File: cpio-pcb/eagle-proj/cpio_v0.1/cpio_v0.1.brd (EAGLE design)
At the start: 100 x 80 mm, 106 parts

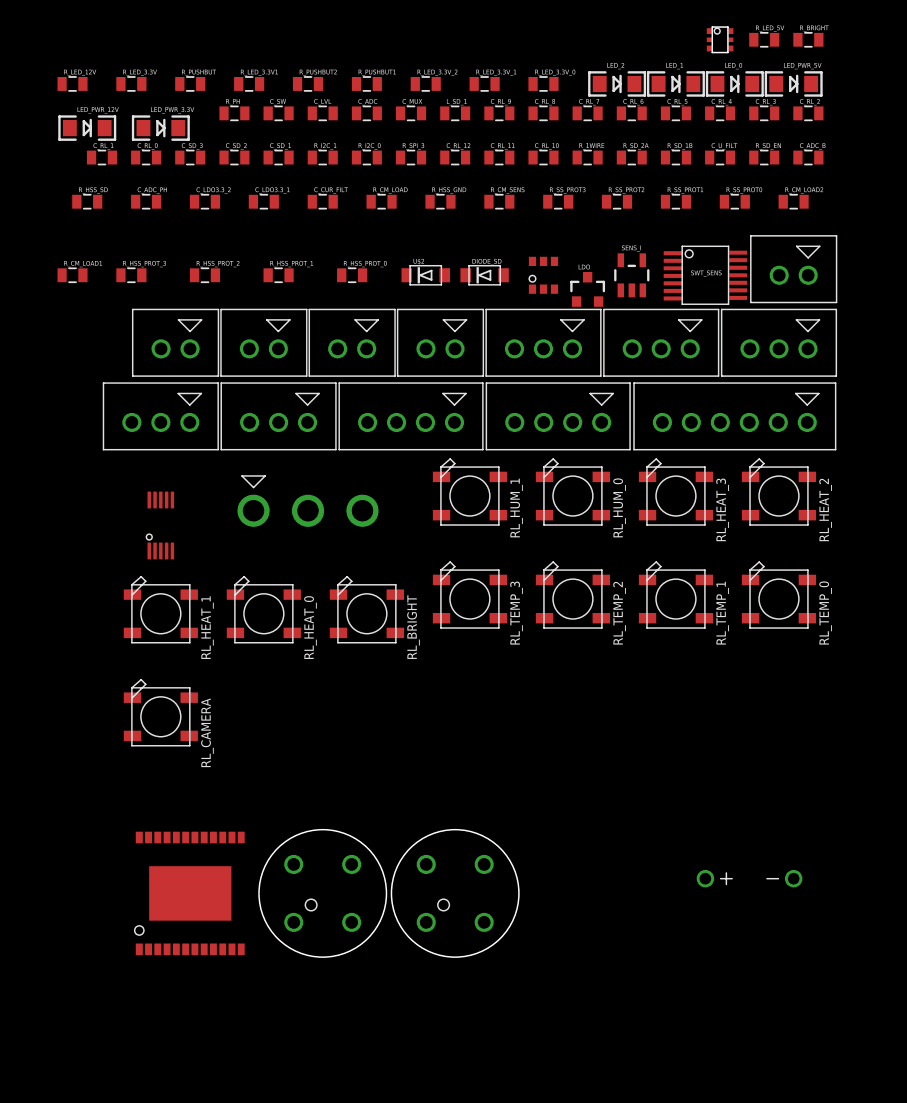
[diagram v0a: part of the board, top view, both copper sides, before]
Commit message: schematic review: button and some R less
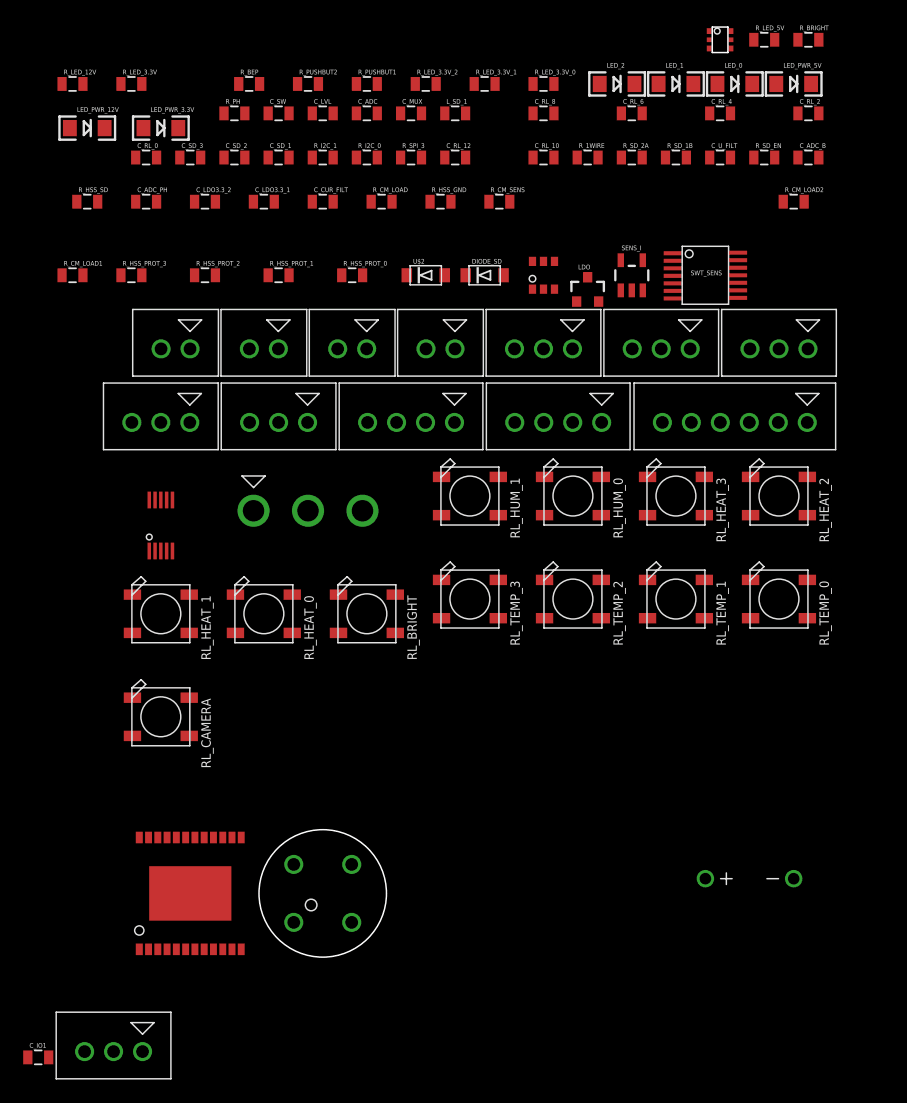
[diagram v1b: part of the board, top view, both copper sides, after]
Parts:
- removed C_RL_1, C_RL_11, C_RL_3, C_RL_5, C_RL_7, C_RL_9: 100n, SparkFun-Passives:0805
- removed PUSH: BUTTON, cpio:BUTTON
- removed R_PUSHBUT: (no value), SparkFun-Passives:0805
- removed R_SS_PROT0, R_SS_PROT1, R_SS_PROT2, R_SS_PROT3: 1k, SparkFun-Passives:0805
- removed SENS_BRIGHT: XH-A-2, cpio:XH-A-2
- added C_IO1: 100n, SparkFun-Passives:0805
- added SENS_PH1: XH-A-3, cpio:XH-A-3
- renumbered R_LED_3.3V1 to R_BEP
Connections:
- removed net GPIO_XXXXX: PUSH.1, PUSH.3
- removed net N$20: R_SS_PROT1.2, SWT_SENS.4
- removed net N$21: R_SS_PROT2.2, SWT_SENS.10
- removed net N$22: R_SS_PROT3.2, SWT_SENS.13
- removed net N$25: C_RL_12.1, R_PUSHBUT2.1
- removed net N$57: PUSH.2, PUSH.4, R_PUSHBUT.1
- new net GPIO_27: C_RL_12.1, R_PUSHBUT1.1, R_PUSHBUT2.2
- net 3.3V: now also C_IO1.1, SENS_PH.1, SENS_PH1.1; no longer R_PUSHBUT.2
- net 5V: no longer C_RL_1.1, C_RL_11.1, C_RL_3.1, C_RL_5.1, C_RL_7.1, C_RL_9.1
- net GND: now also C_IO1.2, SENS_PH.3, SENS_PH1.3; no longer C_RL_1.2, C_RL_11.2, C_RL_3.2, C_RL_5.2, C_RL_7.2, C_RL_9.2, SENS_BRIGHT.2
- net GPIO12: now also SWT_SENS.10; no longer R_SS_PROT2.1
- net GPIO16: now also SWT_SENS.4; no longer R_SS_PROT1.1
- net GPIO20: now also SWT_SENS.1; no longer R_SS_PROT0.1
- net GPIO25: now also SWT_SENS.13; no longer R_SS_PROT3.1
- net N$14: now also RL_HUM_0.4-DIN; no longer R_SS_PROT0.2, SWT_SENS.1
- net N$35: now also SENS_PH1.2; no longer SENS_BRIGHT.1
- net N$5: now also R_PUSHBUT2.1; no longer R_PUSHBUT1.1, R_PUSHBUT2.2
- net N$58: no longer RL_HUM_0.4-DIN
- net N$7: now also SENS_PH.2; no longer SENS_PH.1
